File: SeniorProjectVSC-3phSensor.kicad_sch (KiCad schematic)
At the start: 1 part, among them U1 ATM90E32AS-AU-R

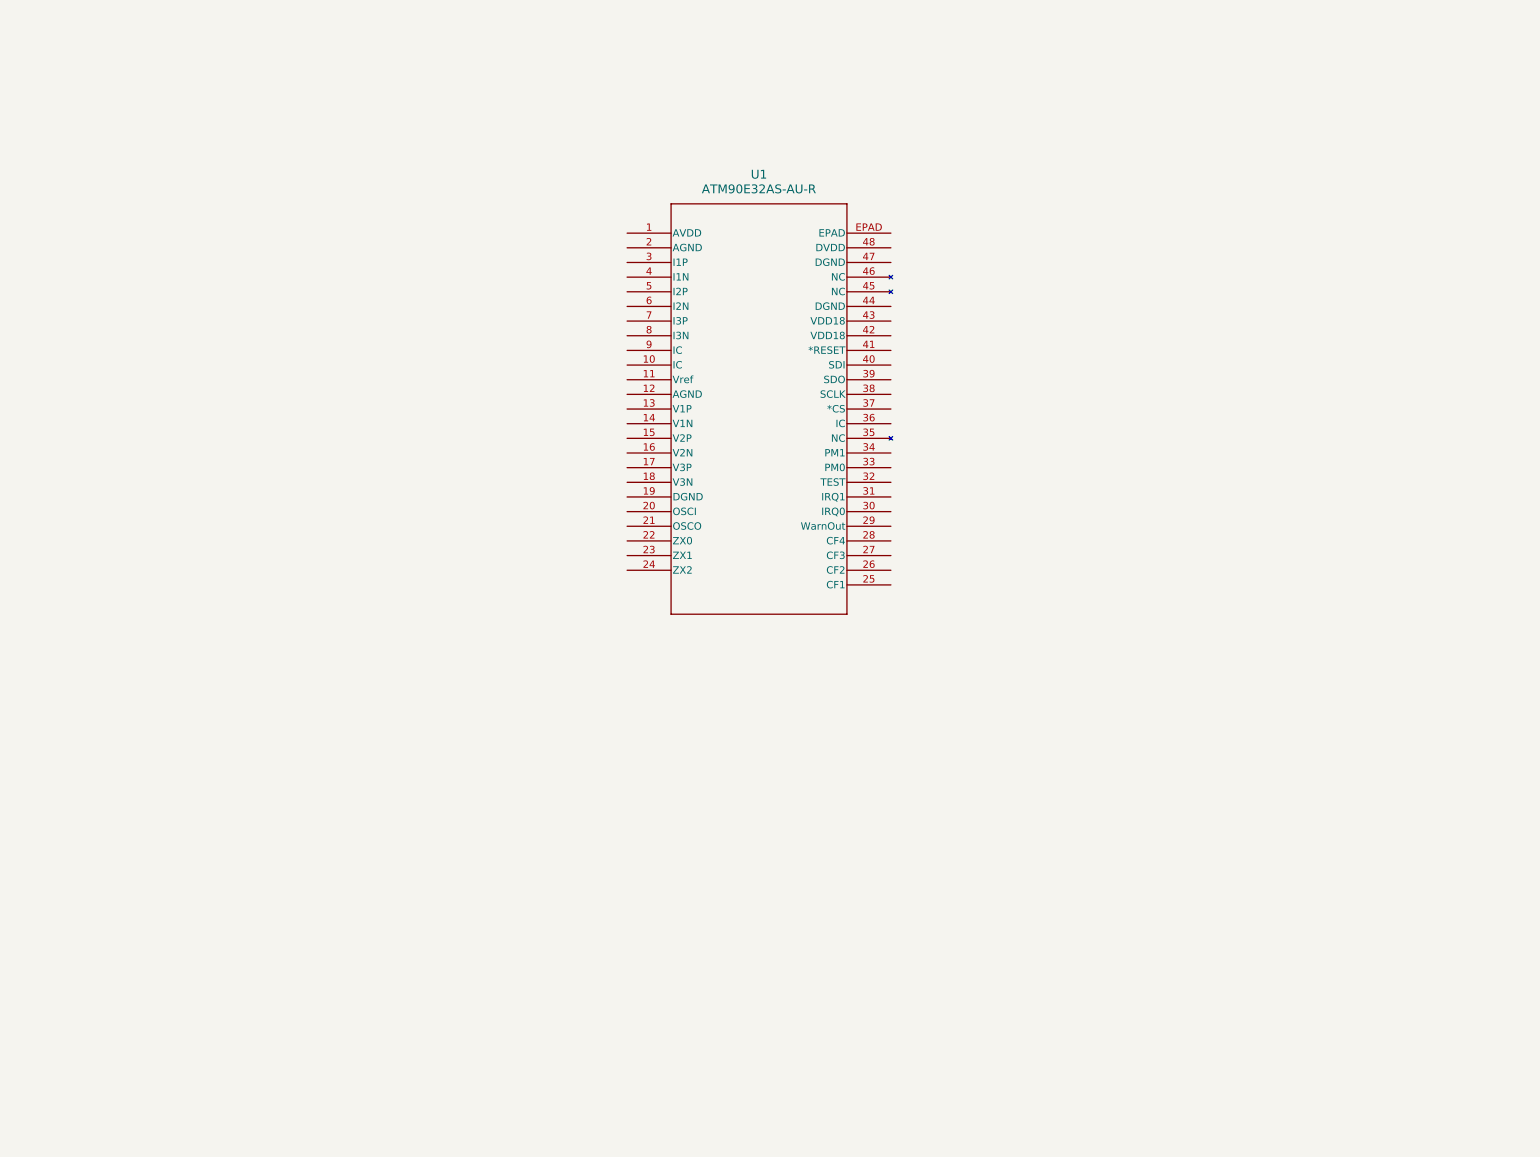
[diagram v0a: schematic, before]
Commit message: Add M90E32AS IC and breakouts
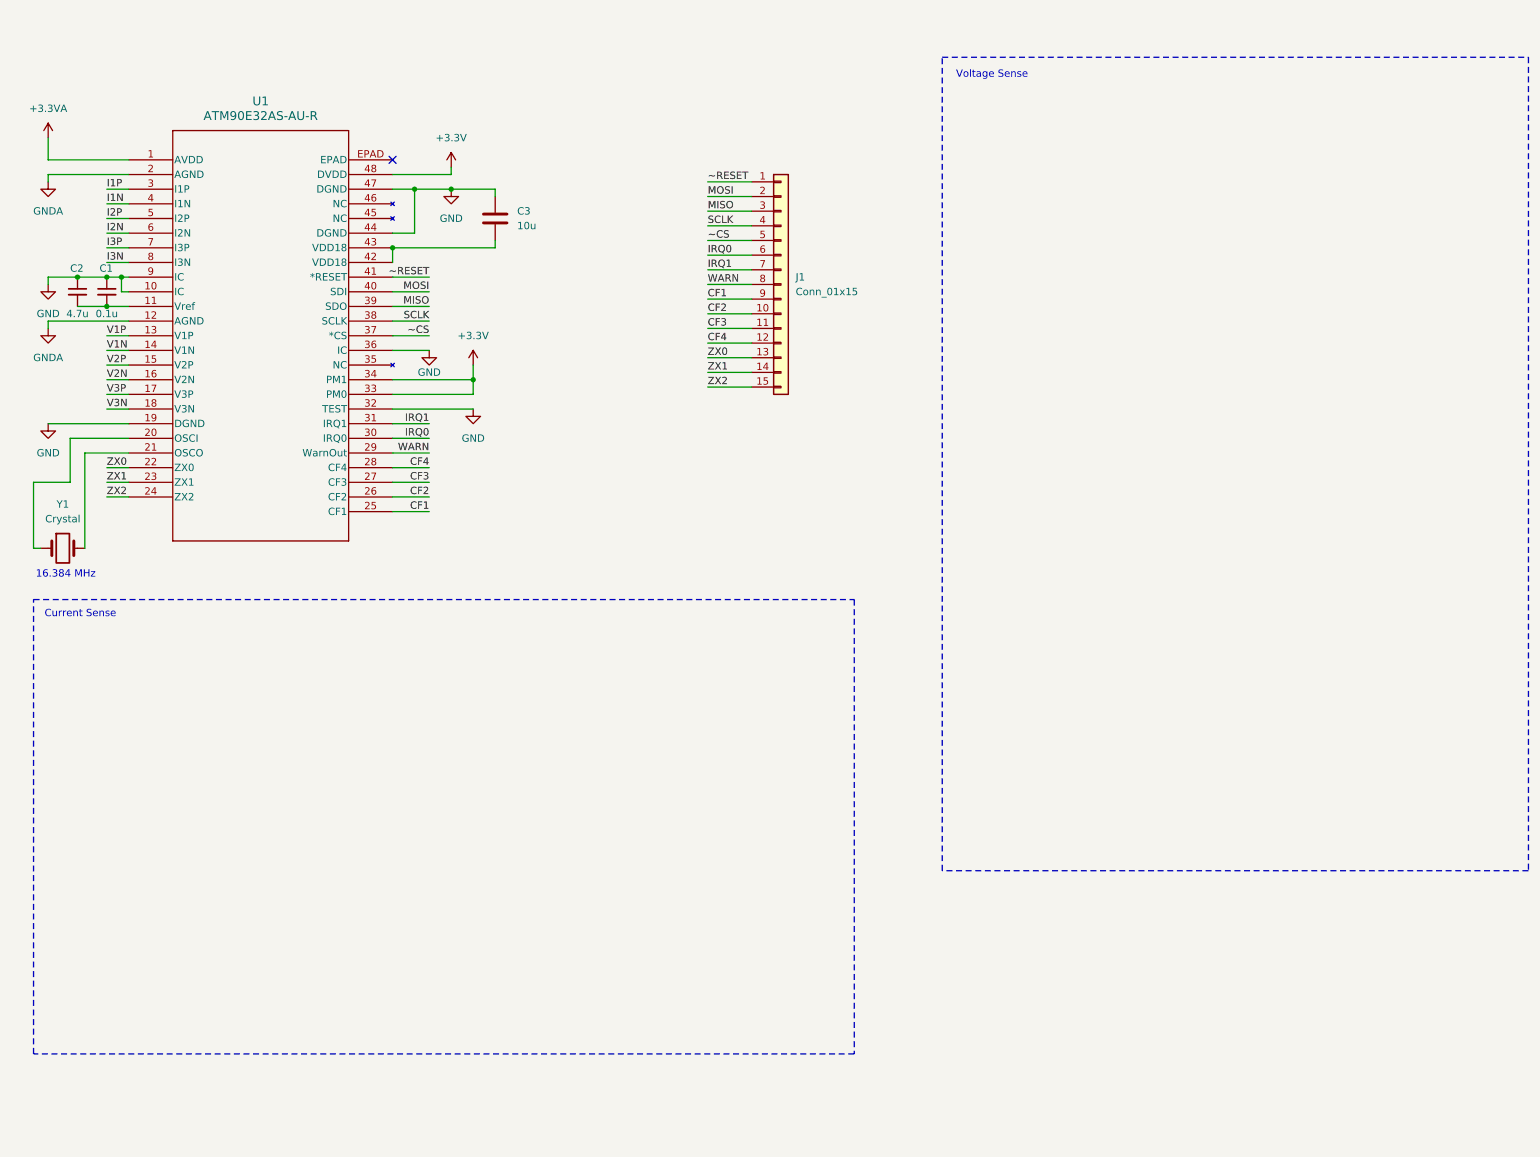
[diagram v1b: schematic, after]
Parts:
- added C1: 0.1u, symbol Device:C_Small
- added C2: 4.7u, symbol Device:C_Small
- added C3: 10u, symbol Device:C
- added J1: Conn_01x15, symbol Connector_Generic:Conn_01x15
- added Y1: Crystal, symbol Device:Crystal
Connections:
- net +3.3VA: now reaches U1.1 (AVDD)
- net GND: now reaches U1.10 (IC)
- net GND: now also U1.19 (DGND), U1.32 (TEST), U1.36 (IC), U1.44 (DGND), U1.47 (DGND), U1.9 (IC), C1.1, C2.1, C3.1
- net at U1.11 (Vref): now also C1.2, C2.2
- net GNDA: now reaches U1.12 (AGND)
- net GNDA: now also U1.2 (AGND)
- net V1P: now reaches U1.13 (V1P)
- net V1N: now reaches U1.14 (V1N)
- net V2P: now reaches U1.15 (V2P)
- net V2N: now reaches U1.16 (V2N)
- net V3P: now reaches U1.17 (V3P)
- net V3N: now reaches U1.18 (V3N)
- net at U1.20 (OSCI): now also Y1.1
- net at U1.21 (OSCO): now also Y1.2
- net ZX0: now reaches U1.22 (ZX0)
- net ZX0: now also J1.13 (Pin_13)
- net ZX1: now reaches U1.23 (ZX1)
- net ZX1: now also J1.14 (Pin_14)
- net ZX2: now reaches U1.24 (ZX2)
- net ZX2: now also J1.15 (Pin_15)
- net CF1: now reaches U1.25 (CF1)
- net CF1: now also J1.9 (Pin_9)
- net CF2: now reaches U1.26 (CF2)
- net CF2: now also J1.10 (Pin_10)
- net CF3: now reaches U1.27 (CF3)
- net CF3: now also J1.11 (Pin_11)
- net CF4: now reaches U1.28 (CF4)
- net CF4: now also J1.12 (Pin_12)
- net WARN: now reaches U1.29 (WarnOut)
- net WARN: now also J1.8 (Pin_8)
- net I1P: now reaches U1.3 (I1P)
- net IRQ0: now reaches U1.30 (IRQ0)
- net IRQ0: now also J1.6 (Pin_6)
- net IRQ1: now reaches U1.31 (IRQ1)
- net IRQ1: now also J1.7 (Pin_7)
- net +3.3V: now reaches U1.33 (PM0)
- net +3.3V: now also U1.34 (PM1), U1.48 (DVDD)
- net ~CS: now reaches U1.37 (*CS)
- net ~CS: now also J1.5 (Pin_5)
- net SCLK: now reaches U1.38 (SCLK)
- net SCLK: now also J1.4 (Pin_4)
- net MISO: now reaches U1.39 (SDO)
- net MISO: now also J1.3 (Pin_3)
- net I1N: now reaches U1.4 (I1N)
- net MOSI: now reaches U1.40 (SDI)
- net MOSI: now also J1.2 (Pin_2)
- net ~RESET: now reaches U1.41 (*RESET)
- net ~RESET: now also J1.1 (Pin_1)
- net at U1.42 (VDD18): now also U1.43 (VDD18), C3.2
- net I2P: now reaches U1.5 (I2P)
- net I2N: now reaches U1.6 (I2N)
- net I3P: now reaches U1.7 (I3P)
- net I3N: now reaches U1.8 (I3N)
- no-connect marks 0 -> 1
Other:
- note added: "16.384 MHz"
- note added: "Current Sense"
- note added: "Voltage Sense"
- title: (none) -> 3-phase Power Sensor
- moved on the sheet: U1

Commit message: Add voltage and current sensors
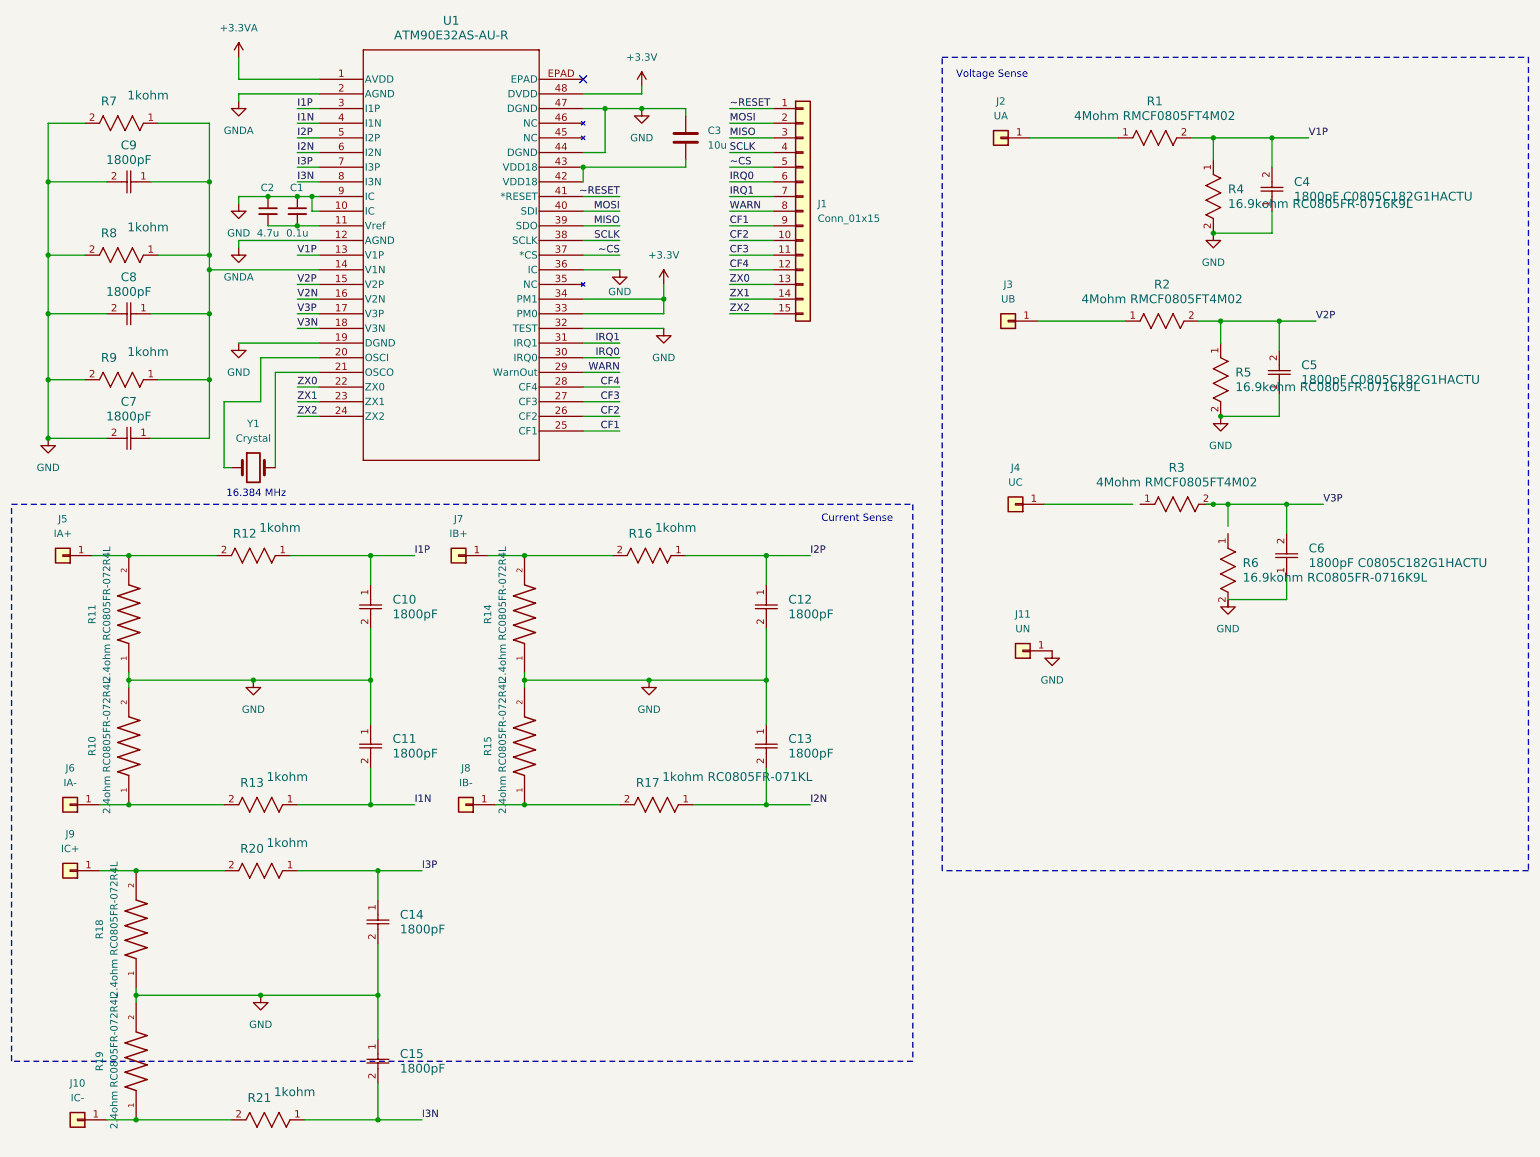
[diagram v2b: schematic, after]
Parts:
- added C10, C11, C12, C13, C14, C15, C7, C8, C9: 1800pF, CAPC220145_100N_KEM, symbol 2024-04-10_05-09-13:C0805C182G1HACTU
- added C4, C5, C6: 1800pF C0805C182G1HACTU, CAPC220145_100N_KEM, symbol 2024-04-10_05-09-13:C0805C182G1HACTU
- added J10: IC-, symbol Connector_Generic:Conn_01x01
- added J11: UN, symbol Connector_Generic:Conn_01x01
- added J2: UA, symbol Connector_Generic:Conn_01x01
- added J3: UB, symbol Connector_Generic:Conn_01x01
- added J4: UC, symbol Connector_Generic:Conn_01x01
- added J5: IA+, symbol Connector_Generic:Conn_01x01
- added J6: IA-, symbol Connector_Generic:Conn_01x01
- added J7: IB+, symbol Connector_Generic:Conn_01x01
- added J8: IB-, symbol Connector_Generic:Conn_01x01
- added J9: IC+, symbol Connector_Generic:Conn_01x01
- added R1, R2, R3: 4Mohm RMCF0805FT4M02, RES_RMCF0805_STP, symbol 2024-04-10_23-25-15:RMCF0805FT4M02
- added R10, R11, R14, R15, R18, R19: 2.4ohm RC0805FR-072R4L, RC0805FR-072R4L:RESC2012X60N, symbol RC0805FR-072R4L:RC0805FR-072R4L
- added R12, R13, R16, R20, R21, R7, R8, R9: 1kohm, RC0805N_YAG, symbol 2024-04-10_04-58-52:RC0805FR-071KL
- added R17: 1kohm RC0805FR-071KL, RC0805N_YAG, symbol 2024-04-10_04-58-52:RC0805FR-071KL
- added R4, R5, R6: 16.9kohm RC0805FR-0716K9L, RC0805N_YAG, symbol 2024-04-10_23-30-45:RC0805FR-0716K9L
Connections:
- net GND: now also C10.2, C11.1, C12.2, C13.1, C14.2, C15.1, C4.1, C5.1, C6.1, C7.2, C8.2, C9.2, J11.1 (Pin_1), R10.2, R11.1, R14.1, R15.2, R18.1, R19.2, R4.2, R5.2, R7.2, R8.2, R9.2
- net I1N: now also C11.2, R13.1
- net I1P: now also C10.1, R12.1
- net I2N: now also C13.2, R17.1
- net I2P: now also C12.1, R16.1
- net I3N: now also C15.2, R21.1
- net I3P: now also C14.1, R20.1
- net V1P: now also C4.2, R1.2, R4.1
- net V2P: now also C5.2, R2.2, R5.1
- net V3P: now also C6.2, R3.2
- net V1N: no longer names the net of U1.14 (V1N)
- net V1N: now also C7.1, C8.1, C9.1, R7.1, R8.1, R9.1
- new net: J9.1 (Pin_1), R18.2, R20.2
- new net: J7.1 (Pin_1), R14.2, R16.2
- new net: J8.1 (Pin_1), R15.1, R17.2
- new net: J5.1 (Pin_1), R11.2, R12.2
- new net: J6.1 (Pin_1), R10.1, R13.2
- new net: J10.1 (Pin_1), R19.1, R21.2
- new net: J2.1 (Pin_1), R1.1
- new net: J3.1 (Pin_1), R2.1
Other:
- moved on the sheet: C1, C2, C3, J1, U1, Y1

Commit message: Modularize schematic and add DC voltage and current sense
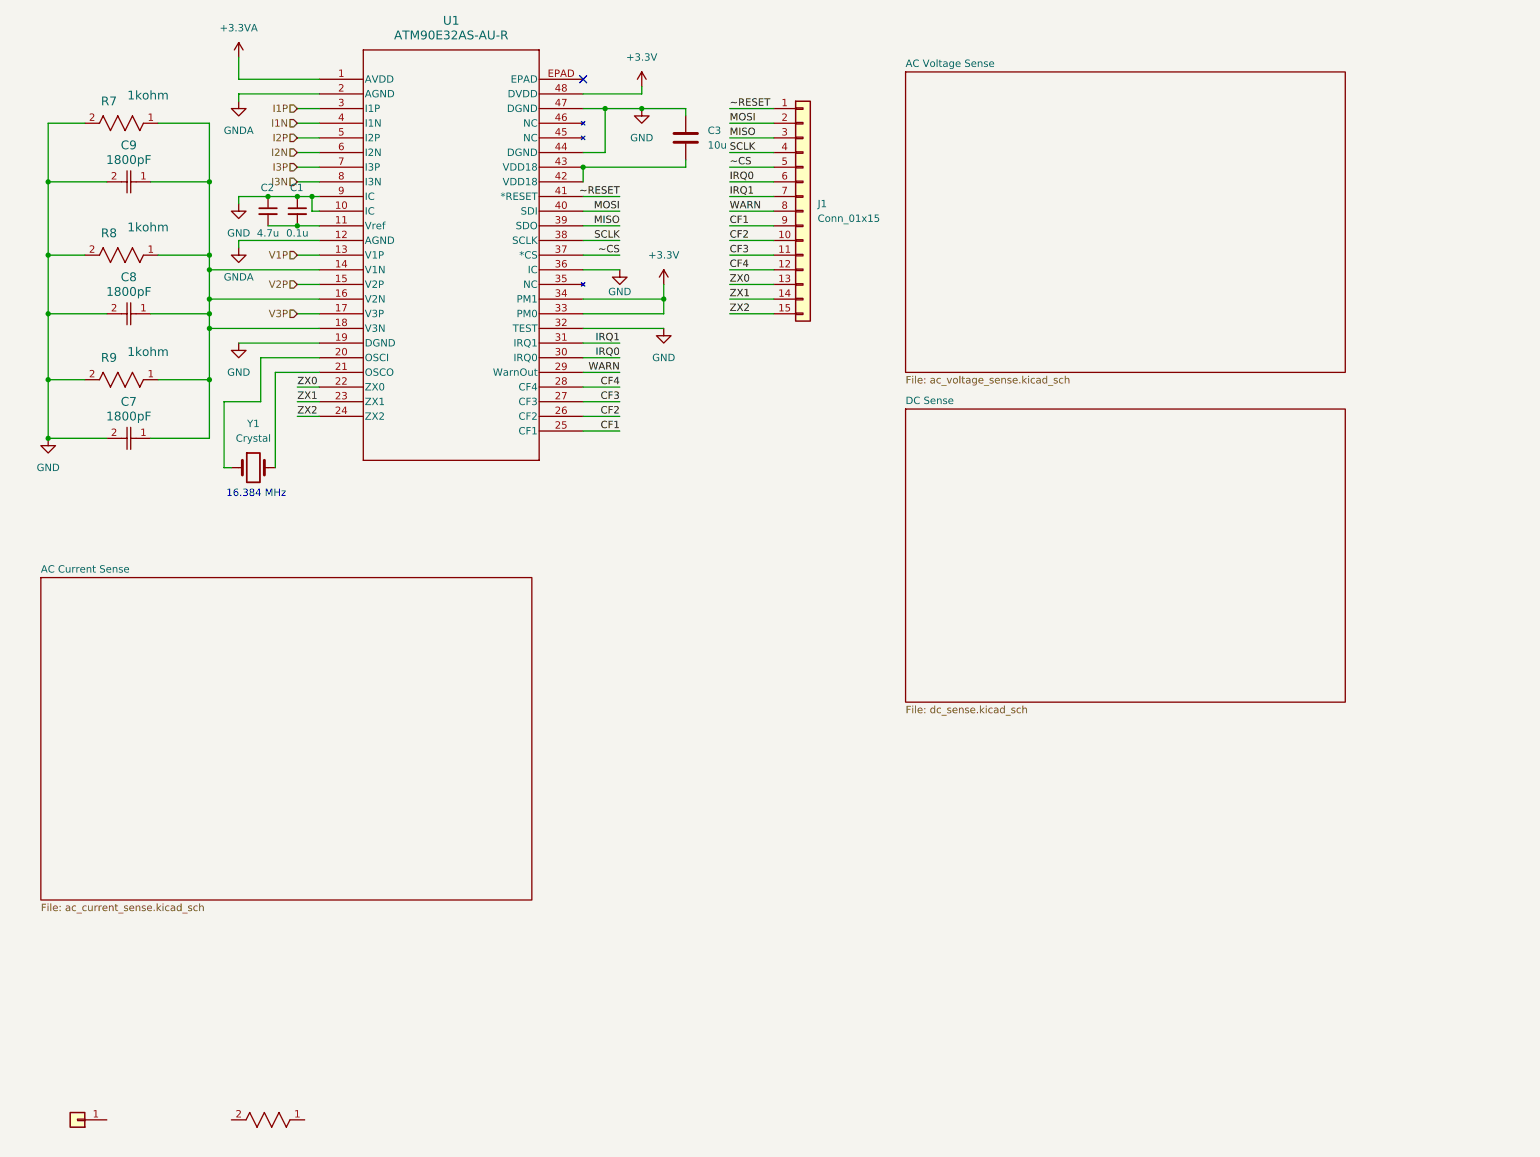
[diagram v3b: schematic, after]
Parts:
- removed C10, C11, C12, C13, C14, C15: 1800pF, CAPC220145_100N_KEM, symbol 2024-04-10_05-09-13:C0805C182G1HACTU
- removed C4, C5, C6: 1800pF C0805C182G1HACTU, CAPC220145_100N_KEM, symbol 2024-04-10_05-09-13:C0805C182G1HACTU
- removed J11: UN, symbol Connector_Generic:Conn_01x01
- removed J2: UA, symbol Connector_Generic:Conn_01x01
- removed J3: UB, symbol Connector_Generic:Conn_01x01
- removed J4: UC, symbol Connector_Generic:Conn_01x01
- removed J5: IA+, symbol Connector_Generic:Conn_01x01
- removed J6: IA-, symbol Connector_Generic:Conn_01x01
- removed J7: IB+, symbol Connector_Generic:Conn_01x01
- removed J8: IB-, symbol Connector_Generic:Conn_01x01
- removed J9: IC+, symbol Connector_Generic:Conn_01x01
- removed R1, R2, R3: 4Mohm RMCF0805FT4M02, RES_RMCF0805_STP, symbol 2024-04-10_23-25-15:RMCF0805FT4M02
- removed R10, R11, R14, R15, R18, R19: 2.4ohm RC0805FR-072R4L, RC0805FR-072R4L:RESC2012X60N, symbol RC0805FR-072R4L:RC0805FR-072R4L
- removed R12, R13, R16, R20: 1kohm, RC0805N_YAG, symbol 2024-04-10_04-58-52:RC0805FR-071KL
- removed R17: 1kohm RC0805FR-071KL, RC0805N_YAG, symbol 2024-04-10_04-58-52:RC0805FR-071KL
- removed R4, R5, R6: 16.9kohm RC0805FR-0716K9L, RC0805N_YAG, symbol 2024-04-10_23-30-45:RC0805FR-0716K9L
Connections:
- net V2N is gone; now on an unnamed net: U1.16 (V2N)
- net V3N is gone; now on an unnamed net: U1.18 (V3N)
- net I3N: no longer R21.1
- net at J10.1 (Pin_1): no longer R21.2
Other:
- added sheet AC Current Sense (ac_current_sense.kicad_sch)
- added sheet AC Voltage Sense (ac_voltage_sense.kicad_sch)
- added sheet DC Sense (dc_sense.kicad_sch)
- note removed: "Current Sense"
- note removed: "Voltage Sense"

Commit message: PCB V1
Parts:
- removed J10: IC-, symbol Connector_Generic:Conn_01x01
- removed R21: 1kohm, RC0805N_YAG, symbol 2024-04-10_04-58-52:RC0805FR-071KL
- added J17: GND Jack, Connector:Banana_Jack_1Pin, symbol Connector_Generic:Conn_01x01
- added J18: +3.3V, Connector_PinHeader_2.54mm:PinHeader_1x01_P2.54mm_Vertical, symbol Connector_Generic:Conn_01x01
- added J19: GND Header, Connector_PinHeader_2.54mm:PinHeader_1x01_P2.54mm_Vertical, symbol Connector_Generic:Conn_01x01
- C1, C2, C3: footprint (none) -> Capacitor_SMD:C_0805_2012Metric_Pad1.18x1.45mm_HandSolder
- C7, C8, C9: footprint CAPC220145_100N_KEM -> Capacitor_SMD:C_0805_2012Metric_Pad1.18x1.45mm_HandSolder
- J1: value Conn_01x15 -> AC Sensor Header; footprint (none) -> Connector_PinHeader_2.54mm:PinHeader_1x15_P2.54mm_Vertical
- R7, R8, R9: footprint RC0805N_YAG -> Resistor_SMD:R_0805_2012Metric_Pad1.20x1.40mm_HandSolder
- U1: footprint TQFP48_7x7MC_MCH -> ATM90E32AS_AU_R:TQFP48_7x7MC_MCH-M
- Y1: footprint (none) -> ABLS_16_384MHZ_B4_T:XTAL_ABLS-16.384MHZ-B4-T
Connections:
- net +3.3V: now also J18.1 (Pin_1)
- net GND: now also U1.2 (AGND), J17.1 (Pin_1), J19.1 (Pin_1)
- net GNDA: no longer U1.2 (AGND)
- new net: C7.1, R9.1, U1.18 (V3N)
- new net: C8.1, R8.1, U1.16 (V2N)
- new net: C9.1, R7.1, U1.14 (V1N)
